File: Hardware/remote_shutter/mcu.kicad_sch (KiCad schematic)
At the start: 31 parts, among them J4 Buzzer, U2 ESP32-PICO-MINI-02, Y1 NX3215SA-32.768K-STD-MUA-14

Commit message: Removed redundant pullups
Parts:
- removed R19, R20, R21, R23, R24, R25: 10k, Resistor_SMD:R_0603_1608Metric_Pad0.98x0.95mm_HandSolder, symbol Device:R_Small
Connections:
- net A3: now also U2.16 (IO26); no longer U2.27 (IO7), U2.9 (I34)
- net B3: no longer names the net of U2.10 (I35)
- net B3: no longer U2.28 (IO8)
- net C3: no longer names the net of U2.4 (I36)

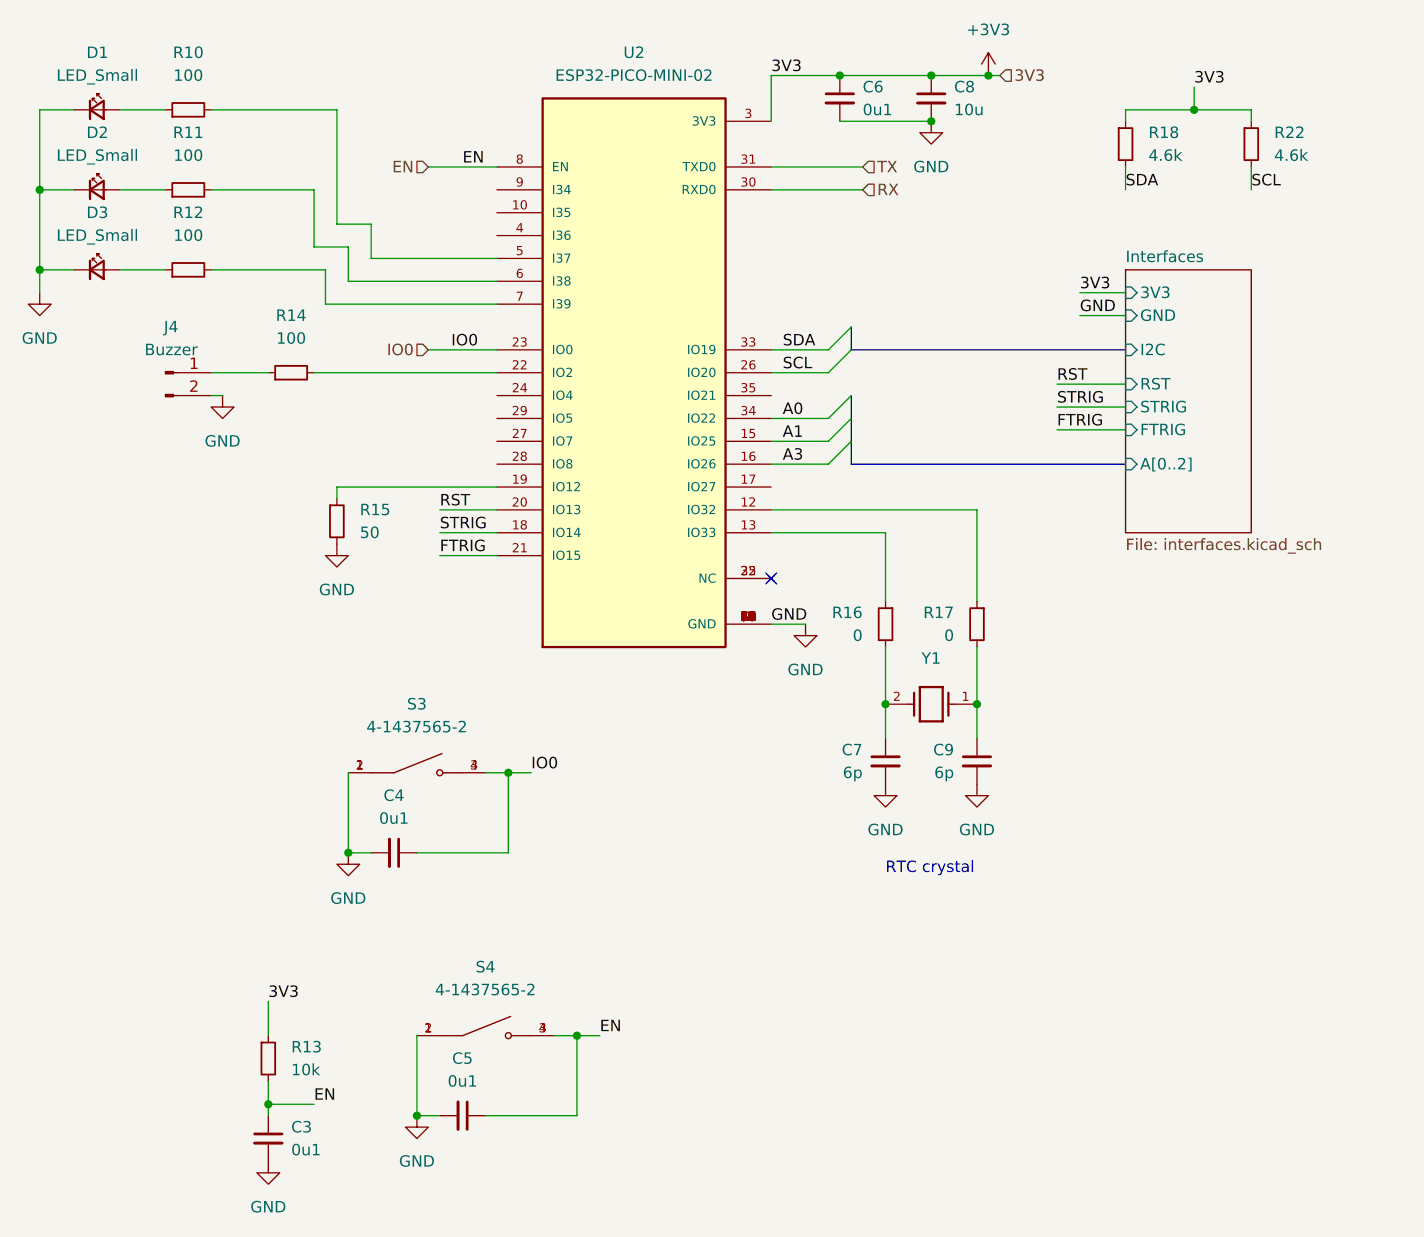
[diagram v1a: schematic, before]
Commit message: Further routing. Fixed I2C net connection.
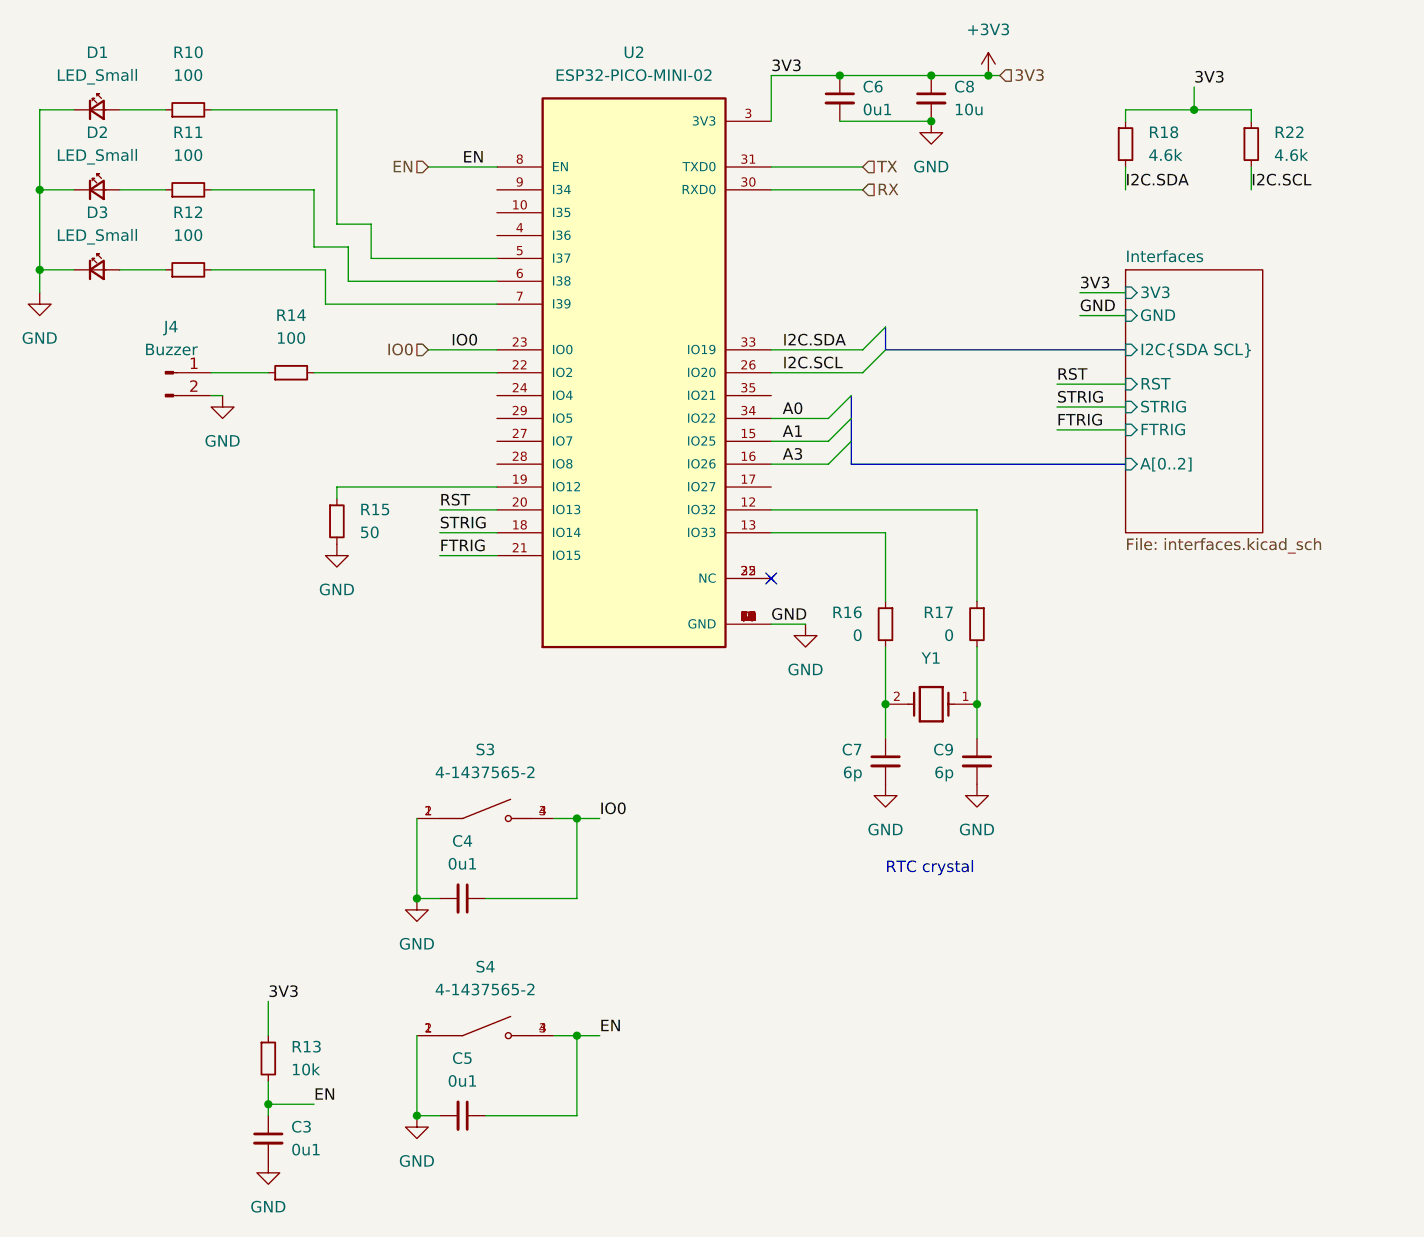
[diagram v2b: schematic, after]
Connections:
- net SCL renamed I2C.SCL
- net SDA renamed I2C.SDA
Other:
- sheet Interfaces ports: added I2C{SDA SCL}; removed I2C
- moved on the sheet: C4, S3
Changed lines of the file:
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@@
 (kicad_sch (version 20211123) (generator eeschema)
   (paper "A4")
-  (junction (at 104.14 132.08) (diameter 0) (color 0 0 0 0)
+  (junction (at 111.76 137.16) (diameter 0) (color 0 0 0 0)
   )
   (junction (at 95.25 160.02) (diameter 0) (color 0 0 0 0)
@@
   (junction (at 168.91 50.8) (diameter 0) (color 0 0 0 0)
   )
-  (junction (at 121.92 123.19) (diameter 0) (color 0 0 0 0)
+  (junction (at 129.54 128.27) (diameter 0) (color 0 0 0 0)
   )
   (junction (at 173.99 115.57) (diameter 0) (color 0 0 0 0)
@@
     (stroke (width 0) (type default) (color 0 0 0 0))
   )
-  (bus_entry (at 157.48 78.74) (size 2.54 -2.54)
-    (stroke (width 0) (type default) (color 0 0 0 0))
-  )
-  (bus_entry (at 157.48 76.2) (size 2.54 -2.54)
+  (bus_entry (at 161.29 76.2) (size 2.54 -2.54)
+    (stroke (width 0) (type default) (color 0 0 0 0))
+  )
+  (bus_entry (at 161.29 78.74) (size 2.54 -2.54)
     (stroke (width 0) (type default) (color 0 0 0 0))
   )
@@
     (stroke (width 0) (type default) (color 0 0 0 0))
   )
-  (wire (pts (xy 121.92 132.08) (xy 121.92 123.19))
+  (wire (pts (xy 129.54 137.16) (xy 129.54 128.27))
     (stroke (width 0) (type default) (color 0 0 0 0))
   )
@@
     (stroke (width 0) (type default) (color 0 0 0 0))
   )
-  (wire (pts (xy 121.92 123.19) (xy 124.46 123.19))
+  (wire (pts (xy 129.54 128.27) (xy 132.08 128.27))
     (stroke (width 0) (type default) (color 0 0 0 0))
   )
@@
     (stroke (width 0) (type default) (color 0 0 0 0))
   )
-  (wire (pts (xy 111.76 132.08) (xy 121.92 132.08))
+  (wire (pts (xy 119.38 137.16) (xy 129.54 137.16))
     (stroke (width 0) (type default) (color 0 0 0 0))
   )
@@
     (stroke (width 0) (type default) (color 0 0 0 0))
   )
-  (bus (pts (xy 160.02 73.66) (xy 160.02 76.2))
+  (bus (pts (xy 163.83 73.66) (xy 163.83 76.2))
     (stroke (width 0) (type default) (color 0 0 0 0))
   )
@@
     (stroke (width 0) (type default) (color 0 0 0 0))
   )
-  (bus (pts (xy 160.02 76.2) (xy 190.5 76.2))
+  (bus (pts (xy 163.83 76.2) (xy 190.5 76.2))
     (stroke (width 0) (type default) (color 0 0 0 0))
   )
@@
     (stroke (width 0) (type default) (color 0 0 0 0))
   )
-  (wire (pts (xy 151.13 76.2) (xy 157.48 76.2))
+  (wire (pts (xy 151.13 76.2) (xy 161.29 76.2))
     (stroke (width 0) (type default) (color 0 0 0 0))
   )
@@
     (stroke (width 0) (type default) (color 0 0 0 0))
   )
-  (wire (pts (xy 104.14 132.08) (xy 104.14 123.19))
+  (wire (pts (xy 111.76 137.16) (xy 111.76 128.27))
     (stroke (width 0) (type default) (color 0 0 0 0))
   )
@@
     (stroke (width 0) (type default) (color 0 0 0 0))
   )
-  (wire (pts (xy 106.68 132.08) (xy 104.14 132.08))
+  (wire (pts (xy 114.3 137.16) (xy 111.76 137.16))
     (stroke (width 0) (type default) (color 0 0 0 0))
   )
@@
     (stroke (width 0) (type default) (color 0 0 0 0))
   )
-  (wire (pts (xy 119.38 123.19) (xy 121.92 123.19))
+  (wire (pts (xy 127 128.27) (xy 129.54 128.27))
     (stroke (width 0) (type default) (color 0 0 0 0))
   )
@@
     (stroke (width 0) (type default) (color 0 0 0 0))
   )
-  (wire (pts (xy 151.13 78.74) (xy 157.48 78.74))
+  (wire (pts (xy 151.13 78.74) (xy 161.29 78.74))
     (stroke (width 0) (type default) (color 0 0 0 0))
   )
@@
     (effects (font (size 1.27 1.27)) (justify left bottom))
   )
-  (label "IO0" (at 124.46 123.19 0)
+  (label "IO0" (at 132.08 128.27 0)
     (effects (font (size 1.27 1.27)) (justify left bottom))
   )
@@
     (effects (font (size 1.27 1.27)) (justify left bottom))
   )
-  (label "SCL" (at 204.47 58.42 0)
-    (effects (font (size 1.27 1.27)) (justify left bottom))
-  )
   (label "EN" (at 132.08 152.4 0)
     (effects (font (size 1.27 1.27)) (justify left bottom))
@@
     (effects (font (size 1.27 1.27)) (justify left bottom))
   )
-  (label "SDA" (at 152.4 76.2 0)
-    (effects (font (size 1.27 1.27)) (justify left bottom))
-  )
-  (label "SDA" (at 190.5 58.42 0)
+  (label "I2C.SDA" (at 152.4 76.2 0)
+    (effects (font (size 1.27 1.27)) (justify left bottom))
+  )
+  (label "I2C.SDA" (at 190.5 58.42 0)
     (effects (font (size 1.27 1.27)) (justify left bottom))
   )
@@
     (effects (font (size 1.27 1.27)) (justify left bottom))
   )
+  (label "I2C.SCL" (at 204.47 58.42 0)
+    (effects (font (size 1.27 1.27)) (justify left bottom))
+  )
   (label "STRIG" (at 182.88 82.55 0)
     (effects (font (size 1.27 1.27)) (justify left bottom))
@@
     (effects (font (size 1.27 1.27)) (justify left bottom))
   )
-  (label "SCL" (at 152.4 78.74 0)
+  (label "I2C.SCL" (at 152.4 78.74 0)
     (effects (font (size 1.27 1.27)) (justify left bottom))
   )
@@
     (pin "2")
   )
-  (symbol (lib_id "4-1437565-2:4-1437565-2") (at 111.76 123.19 0) (unit 1)
-    (in_bom yes) (on_board yes) (fields_autoplaced)
-    (property "Reference" "S3" (id 0) (at 111.76 115.57 0))
-    (property "Value" "4-1437565-2" (id 1) (at 111.76 118.11 0))
-    (property "Footprint" "footprint:SW_4-1437565-2" (id 2) (at 111.76 123.19 0)
-      (effects (font (size 1.27 1.27)) (justify bottom) hide)
-    )
-    (property "Datasheet" "" (id 3) (at 111.76 123.19 0)
-      (effects (font (size 1.27 1.27)) hide)
-    )
-    (property "EU_RoHS_Compliance" "Compliant" (id 4) (at 111.76 123.19 0)
-      (effects (font (size 1.27 1.27)) (justify bottom) hide)
-    )
-    (property "Comment" "4-1437565-2" (id 5) (at 111.76 123.19 0)
+  (symbol (lib_id "4-1437565-2:4-1437565-2") (at 119.38 128.27 0) (unit 1)
+    (in_bom yes) (on_board yes) (fields_autoplaced)
+    (property "Reference" "S3" (id 0) (at 119.38 120.65 0))
+    (property "Value" "4-1437565-2" (id 1) (at 119.38 123.19 0))
+    (property "Footprint" "footprint:SW_4-1437565-2" (id 2) (at 119.38 128.27 0)
+      (effects (font (size 1.27 1.27)) (justify bottom) hide)
+    )
+    (property "Datasheet" "" (id 3) (at 119.38 128.27 0)
+      (effects (font (size 1.27 1.27)) hide)
+    )
+    (property "EU_RoHS_Compliance" "Compliant" (id 4) (at 119.38 128.27 0)
+      (effects (font (size 1.27 1.27)) (justify bottom) hide)
+    )
+    (property "Comment" "4-1437565-2" (id 5) (at 119.38 128.27 0)
       (effects (font (size 1.27 1.27)) (justify bottom) hide)
     )
@@
     (pin "2")
   )
-  (symbol (lib_id "Device:C_Small") (at 109.22 132.08 270) (unit 1)
-    (in_bom yes) (on_board yes) (fields_autoplaced)
-    (property "Reference" "C4" (id 0) (at 109.2136 125.73 90))
-    (property "Value" "0u1" (id 1) (at 109.2136 128.27 90))
-    (property "Footprint" "Capacitor_SMD:C_0603_1608Metric_Pad1.08x0.95mm_HandSolder" (id 2) (at 109.22 132.08 0)
-      (effects (font (size 1.27 1.27)) hide)
-    )
-    (property "Datasheet" "~" (id 3) (at 109.22 132.08 0)
+  (symbol (lib_id "Device:C_Small") (at 116.84 137.16 270) (unit 1)
+    (in_bom yes) (on_board yes) (fields_autoplaced)
+    (property "Reference" "C4" (id 0) (at 116.8336 130.81 90))
+    (property "Value" "0u1" (id 1) (at 116.8336 133.35 90))
+    (property "Footprint" "Capacitor_SMD:C_0603_1608Metric_Pad1.08x0.95mm_HandSolder" (id 2) (at 116.84 137.16 0)
+      (effects (font (size 1.27 1.27)) hide)
+    )
+    (property "Datasheet" "~" (id 3) (at 116.84 137.16 0)
       (effects (font (size 1.27 1.27)) hide)
     )
@@
     (pin "2")
   )
-  (symbol (lib_id "power:GND") (at 104.14 132.08 0) (unit 1)
-    (in_bom yes) (on_board yes) (fields_autoplaced)
-    (property "Reference" "#PWR0107" (id 0) (at 104.14 138.43 0)
-      (effects (font (size 1.27 1.27)) hide)
-    )
-    (property "Value" "GND" (id 1) (at 104.14 137.16 0))
-    (property "Footprint" "" (id 2) (at 104.14 132.08 0)
-      (effects (font (size 1.27 1.27)) hide)
-    )
-    (property "Datasheet" "" (id 3) (at 104.14 132.08 0)
+  (symbol (lib_id "power:GND") (at 111.76 137.16 0) (unit 1)
+    (in_bom yes) (on_board yes) (fields_autoplaced)
+    (property "Reference" "#PWR0107" (id 0) (at 111.76 143.51 0)
+      (effects (font (size 1.27 1.27)) hide)
+    )
+    (property "Value" "GND" (id 1) (at 111.76 142.24 0))
+    (property "Footprint" "" (id 2) (at 111.76 137.16 0)
+      (effects (font (size 1.27 1.27)) hide)
+    )
+    (property "Datasheet" "" (id 3) (at 111.76 137.16 0)
       (effects (font (size 1.27 1.27)) hide)
     )
@@
   )
   (symbol (lib_id "4-1437565-2:4-1437565-2") (at 119.38 152.4 0) (unit 1)
-    (in_bom yes) (on_board yes) (fields_autoplaced)
+    (in_bom yes) (on_board yes)
     (property "Reference" "S4" (id 0) (at 119.38 144.78 0))
     (property "Value" "4-1437565-2" (id 1) (at 119.38 147.32 0))
@@
     (pin "4")
   )
-  (sheet (at 190.5 67.31) (size 13.97 29.21) (fields_autoplaced)
+  (sheet (at 190.5 67.31) (size 15.24 29.21) (fields_autoplaced)
     (stroke (width 0.1524) (type solid) (color 0 0 0 0))
     (fill (color 255 229 191 1.0000))
@@
       (effects (font (size 1.27 1.27)) (justify left))
     )
-    (pin "I2C" input (at 190.5 76.2 180)
-      (effects (font (size 1.27 1.27)) (justify left))
-    )
+    (pin "I2C{SDA SCL}" input (at 190.5 76.2 180)
+      (effects (font (size 1.27 1.27)) (justify left))
+    )

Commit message: Initial routing complete
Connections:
- net A3 renamed A2
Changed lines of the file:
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@@
     (effects (font (size 1.27 1.27)) (justify left bottom))
   )
-  (label "A3" (at 152.4 88.9 0)
+  (label "A2" (at 152.4 88.9 0)
     (effects (font (size 1.27 1.27)) (justify left bottom))
   )
